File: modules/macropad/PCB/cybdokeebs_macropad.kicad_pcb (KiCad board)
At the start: 2 copper layers, 74 parts, among them J13 Conn_01x05_Socket, J14 Conn_01x05_Socket, J16 Conn_01x05_Pin, J9 Conn_01x05_Pin, SW1 BOOTSEL, SW10 SW_Push_45deg, SW11 SW_Push_45deg, SW12 SW_Push_45deg, SW13 SW_Push_45deg, SW14 SW_Push_45deg, SW15 SW_Push_45deg, SW16 SW_Push_45deg, SW17 SW_Push_45deg, SW18 SW_Push_45deg, SW19 SW_Push_45deg, SW2 RESET, SW20 SW_Push_45deg, SW21 SW_Push_45deg, SW22 SW_Push_45deg, SW3 SW_Push_45deg, SW4 SW_Push_45deg, SW5 SW_Push_45deg, SW6 SW_Push_45deg, SW7 SW_Push_45deg, SW8 SW_Push_45deg, SW9 SW_Push_45deg, U2 RP2350_60QFN, U3 BM03B-SRSS-TB

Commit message: macropad finished
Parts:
- removed C16, C17: 100nF, Capacitor_SMD:C_0402_1005Metric_Pad0.74x0.62mm_HandSolder
- added J10: Conn_01x05_Pin, imports:pogo 5pin 2.54, F.Cu at (268.0, 114.0)
- added J11: Conn_01x05_Socket, imports:pogo 5pin 2.54, F.Cu at (193.7, 143.3)
- added J12: Conn_01x05_Socket, imports:pogo 5pin 2.54, F.Cu at (243.7, 143.3)
- added J15: Conn_01x05_Pin, imports:pogo 5pin 2.54, F.Cu at (179.0, 119.0)
- added U1: TCA4307DGKR, easyeda2kicad:VSSOP-8_L3.0-W3.0-P0.65-LS4.9-BL, B.Cu at (211.7, 55.8)
- C1, C10, C11, C12, C13, C14, C15, C2, C3, C4, C5, C6, C7, C8, C9, L1, R10, R2, R3, R4, R6, R7, R8, R9, U2, U3: moved to B.Cu
- D1, D10, D11, D12, D13, D14, D15, D16, D17, D18, D19, D2, D20, D3, D4, D5, D6, D7, D8, D9: value 1N4148 -> 1N4148W; moved to B.Cu
- SW1: footprint Resistor_SMD:R_0402_1005Metric_Pad0.72x0.64mm_HandSolder -> Button_Switch_SMD:SW_Push_SPST_NO_Alps_SKRK; moved to B.Cu
- SW2: value RESET -> BOOTSEL; footprint Resistor_SMD:R_0402_1005Metric_Pad0.72x0.64mm_HandSolder -> Button_Switch_SMD:SW_Push_SPST_NO_Alps_SKRK; moved to B.Cu
- moved D4 221.4 mm to (260.5, 44.1), turned to -90 degrees
- moved D8 202.6 mm to (260.3, 69.4), turned to 90 degrees
- moved D12 202.5 mm to (260.4, 85.4), turned to 90 degrees
- moved D3 202.2 mm to (241.4, 44.1), turned to -90 degrees
- moved SW6 199.5 mm to (252.1, 50.8)
- moved D7 198.8 mm to (241.2, 69.4), turned to 90 degrees
- moved D20 189.7 mm to (260.4, 123.4), turned to 90 degrees
- moved D16 189.7 mm to (260.4, 104.4), turned to 90 degrees
- moved D11 183.1 mm to (241.3, 85.4), turned to 90 degrees
- moved D2 183.0 mm to (222.4, 44.1), turned to -90 degrees
- moved SW10 180.1 mm to (252.1, 69.8)
- moved D6 179.6 mm to (222.2, 69.4), turned to 90 degrees
- moved SW5 178.2 mm to (233.1, 50.8)
- moved D19 170.9 mm to (241.4, 123.4), turned to 90 degrees
- moved D15 170.7 mm to (241.4, 104.4), turned to 90 degrees
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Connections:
- net Net-(J13-Pin_2) renamed /minimum_system/0-1-EN
- net Net-(J13-Pin_3) renamed /minimum_system/0-1-SDA
- net Net-(J13-Pin_4) renamed /minimum_system/0-1-SCL
- net Net-(J14-Pin_2) renamed /minimum_system/0-0-EN
- net Net-(J14-Pin_3) renamed /minimum_system/0-0-SDA
- net Net-(J14-Pin_4) renamed /minimum_system/0-0-SCL
- D1 pad 1: /ROW1 -> GPIO1
- D10 pad 1: /ROW4 -> GPIO10
- D11 pad 1: /ROW3 -> GPIO10
- D12 pad 1: /ROW4 -> GPIO10
- D13 pad 1: /ROW3 -> GPIO2
- D14 pad 1: /ROW4 -> GPIO2
- D15 pad 1: /ROW3 -> GPIO2
- D16 pad 1: /ROW4 -> GPIO2
- D17 pad 1: /ROW5 -> GPIO16
- D18 pad 1: /ROW5 -> GPIO16
- D19 pad 1: /ROW5 -> GPIO16
- D2 pad 1: /ROW1 -> GPIO1
- D20 pad 1: /ROW5 -> GPIO16
- D3 pad 1: /ROW1 -> GPIO1
- D4 pad 1: /ROW1 -> GPIO1
- D5 pad 1: /ROW2 -> GPIO12
- D6 pad 1: /ROW2 -> GPIO12
- D7 pad 1: /ROW2 -> GPIO12
- D8 pad 1: /ROW2 -> GPIO12
- D9 pad 1: /ROW3 -> GPIO10
- SW10 pad 1: /COL4 -> GPIO11
- SW11 pad 1: /COL1 -> GPIO18
- SW12 pad 1: /COL1 -> GPIO17
- SW13 pad 1: /COL2 -> GPIO14
- SW14 pad 1: /COL2 -> GPIO11
- SW15 pad 1: /COL3 -> GPIO18
- SW16 pad 1: /COL3 -> GPIO17
- SW17 pad 1: /COL4 -> GPIO14
- SW18 pad 1: /COL4 -> GPIO11
- SW19 pad 1: /COL1 -> GPIO18
- SW20 pad 1: /COL2 -> GPIO17
- SW21 pad 1: /COL3 -> GPIO14
- SW22 pad 1: /COL4 -> GPIO11
- SW3 pad 1: /COL1 -> GPIO18
- SW4 pad 1: /COL2 -> GPIO17
- SW5 pad 1: /COL3 -> GPIO14
- SW6 pad 1: /COL4 -> GPIO11
- SW7 pad 1: /COL1 -> GPIO18
- SW8 pad 1: /COL2 -> GPIO17
- SW9 pad 1: /COL3 -> GPIO14
- U2 pad 42: GPIO28 -> /minimum_system/SYS_SDA
- U2 pad 43: GPIO29 -> /minimum_system/SYS_SCL
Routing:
- net +3V3: track 0.00 -> 558.2 mm, vias 0 -> 5
- net /minimum_system/0-0-SCL: track 0.00 -> 238.0 mm, vias 0 -> 2
- net /minimum_system/0-0-SDA: track 0.00 -> 232.9 mm, vias 0 -> 1
- net /minimum_system/0-1-EN: track 0.00 -> 210.9 mm, vias 0 -> 2
- net /minimum_system/0-1-SDA: track 0.00 -> 209.4 mm, vias 0 -> 3
- net /minimum_system/0-1-SCL: track 0.00 -> 208.8 mm, vias 0 -> 3
- net /minimum_system/0-0-EN: track 0.00 -> 204.6 mm
- net GPIO16: track 0.00 -> 150.6 mm, vias 0 -> 10
- net GPIO2: track 0.00 -> 129.1 mm, vias 0 -> 8
- net GPIO18: track 0.00 -> 117.1 mm, vias 0 -> 2
- net GPIO10: track 0.00 -> 108.3 mm, vias 0 -> 8
- net GPIO14: track 0.00 -> 101.4 mm, vias 0 -> 2
- net GPIO11: track 0.00 -> 97.9 mm, vias 0 -> 2
- net GPIO17: track 0.00 -> 93.2 mm, vias 0 -> 2
- net GPIO12: track 0.00 -> 74.8 mm, vias 0 -> 7
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- added copper zone on B.Cu, net GND
- added copper zone on F.Cu, net GND
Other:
- board outline added: 94 x 114 mm

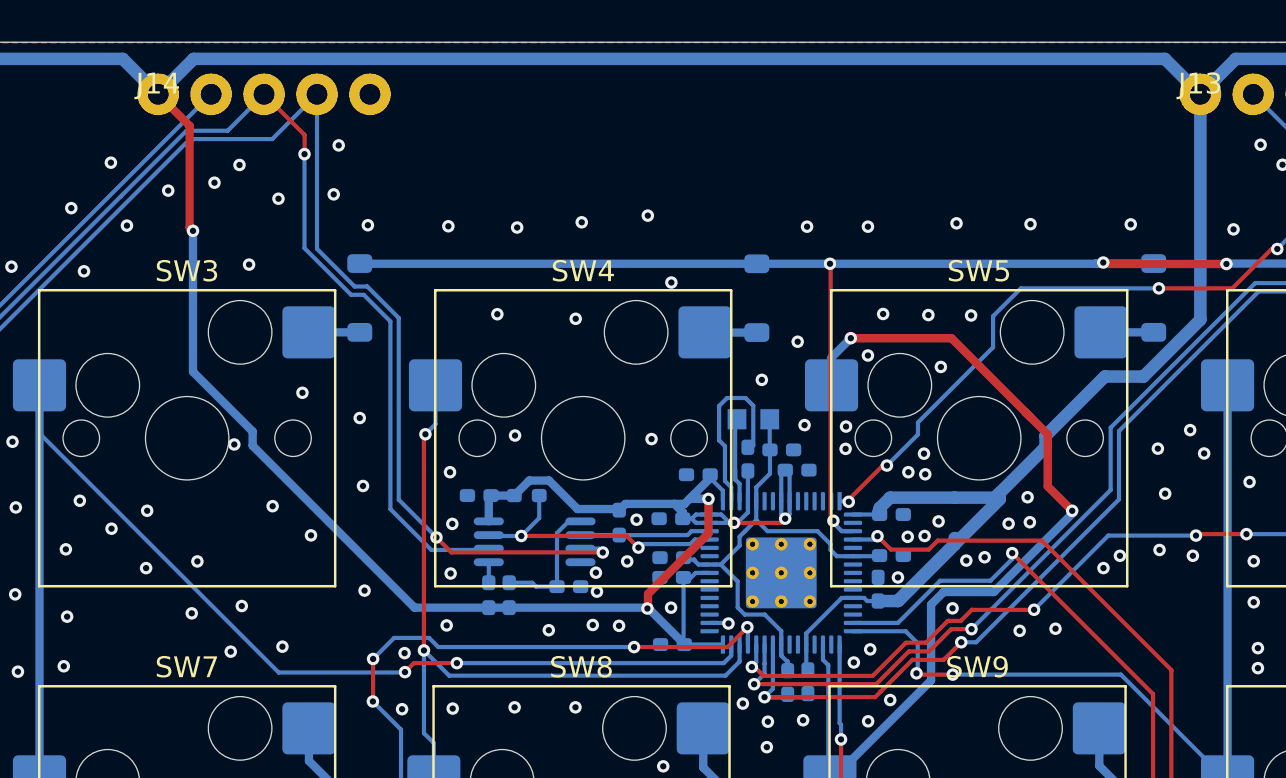
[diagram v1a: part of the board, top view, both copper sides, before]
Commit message: started main keyboard
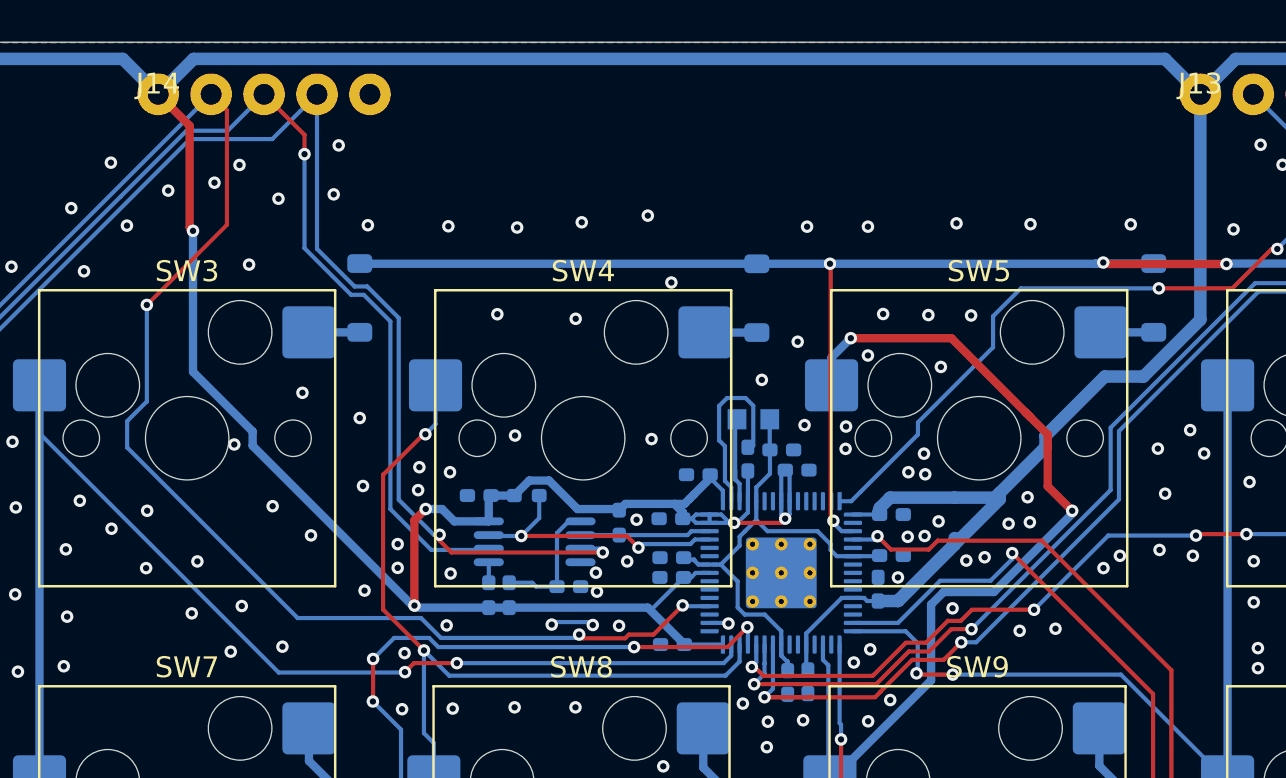
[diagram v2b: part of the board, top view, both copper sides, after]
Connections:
- U2 pad 34: GPIO22 -> /minimum_system/0-0-EN
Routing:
- net /minimum_system/0-0-EN: track 204.6 -> 256.4 mm, vias 0 -> 3
- net GND: track 9.05 -> 11.1 mm, vias 279 -> 281
- net GPIO17: track 93.2 -> 94.8 mm
- net +3V3: track 558.2 -> 557.4 mm
- net /minimum_system/BOOTSEL: track 45.8 -> 45.7 mm, vias 4 -> 2

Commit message: zine!! and cases
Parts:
- added REF**: MountingHole_3.2mm_M3, MountingHole:MountingHole_3.2mm_M3, F.Cu at (223.5, 140.2)
- added REF**: MountingHole_3.2mm_M3, MountingHole:MountingHole_3.2mm_M3, F.Cu at (181.8, 88.8)
- added REF**: MountingHole_3.2mm_M3, MountingHole:MountingHole_3.2mm_M3, F.Cu at (223.5, 36.8)

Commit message: macropad holes line up now
not updated in assembly.step but they line up now
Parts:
- moved J15 5.00 mm to (179.0, 114.0)
- moved J16 5.00 mm to (179.0, 54.0)
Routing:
- net /minimum_system/0-0-SDA: track 232.9 -> 234.1 mm
- net /minimum_system/0-1-SDA: track 209.4 -> 208.5 mm
- net /minimum_system/0-1-SCL: track 208.8 -> 208.1 mm
- net /minimum_system/0-0-SCL: track 238.2 -> 238.8 mm
- net /minimum_system/0-0-EN: track 256.4 -> 257.0 mm
